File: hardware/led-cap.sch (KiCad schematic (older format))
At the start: 11 parts, among them IC1 ATTINY20-X, K1 CONN_3, K2 pgrm_top, K3 pgrm_bot, P1 battery, Q1 IRLML2402PbF, U1 MMA7660

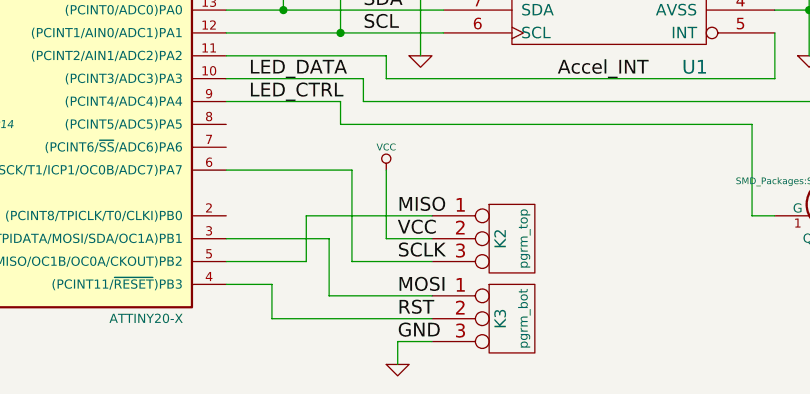
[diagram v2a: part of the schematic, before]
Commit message: Moving parts away from accelerometer
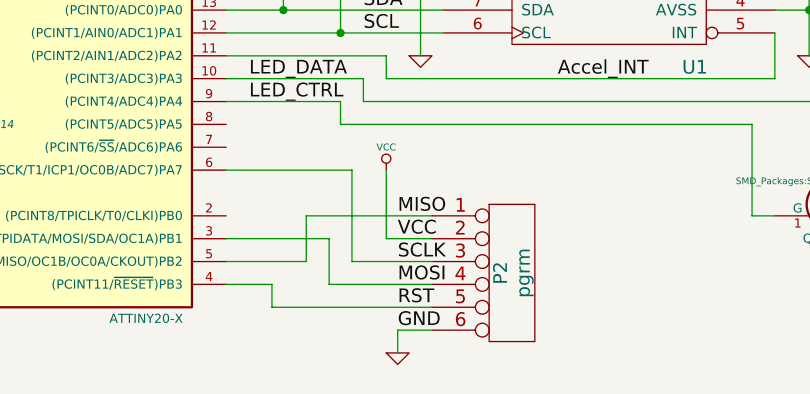
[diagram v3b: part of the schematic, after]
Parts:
- removed K2: pgrm_top, prgm:bcProgramHeader, symbol CONN_3
- removed K3: pgrm_bot, prgm:bcProgramHeader_bottom, symbol CONN_3
- added P2: pgrm, symbol CONN_6
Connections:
- net GND: now also P2.6
- net MISO: now also P2.1
- net MOSI: now also P2.4
- net RST: now also P2.5
- net SCLK: now also P2.3
- net VCC: now also P2.2
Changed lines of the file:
@@
 L GND #PWR07
 U 1 1 54E77FCD
-P 5750 5000
-F 0 "#PWR07" H 5750 5000 30  0001 C CNN
-F 1 "GND" H 5750 4930 30  0001 C CNN
-F 2 "" H 5750 5000 60  0000 C CNN
-F 3 "" H 5750 5000 60  0000 C CNN
-	1    5750 5000
+P 5750 4950
+F 0 "#PWR07" H 5750 4950 30  0001 C CNN
+F 1 "GND" H 5750 4880 30  0001 C CNN
+F 2 "" H 5750 4950 60  0000 C CNN
+F 3 "" H 5750 4950 60  0000 C CNN
+	1    5750 4950
 	1    0    0    -1
 $EndComp
@@
 	1    0    0    -1
 $EndComp
-$Comp
-L CONN_3 K2
-U 1 1 54EDFF11
-P 6250 4450
-F 0 "K2" V 6200 4450 50  0000 C CNN
-F 1 "pgrm_top" V 6300 4450 40  0000 C CNN
-F 2 "prgm:bcProgramHeader" H 6250 4450 60  0001 C CNN
-F 3 "" H 6250 4450 60  0000 C CNN
-	1    6250 4450
-	1    0    0    -1
-$EndComp
-$Comp
-L CONN_3 K3
-U 1 1 54EDFFA4
-P 6250 4800
-F 0 "K3" V 6200 4800 50  0000 C CNN
-F 1 "pgrm_bot" V 6300 4800 40  0000 C CNN
-F 2 "prgm:bcProgramHeader_bottom" H 6250 4800 60  0001 C CNN
-F 3 "" H 6250 4800 60  0000 C CNN
-	1    6250 4800
-	1    0    0    -1
-$EndComp
 Text Label 5600 3450 0    60   ~ 0
 SDA
@@
 Text Label 5750 4350 0    60   ~ 0
 MISO
-Text Label 5750 4700 0    60   ~ 0
+Text Label 5750 4650 0    60   ~ 0
 MOSI
-Text Label 5750 4800 0    60   ~ 0
+Text Label 5750 4750 0    60   ~ 0
 RST
-Text Label 5750 4900 0    60   ~ 0
+Text Label 5750 4850 0    60   ~ 0
 GND
 Text Label 5750 4450 0    60   ~ 0
@@
 	5550 4150 5000 4150
 Wire Wire Line
-	5900 4700 5450 4700
-Wire Wire Line
-	5450 4700 5450 4450
+	5900 4650 5450 4650
+Wire Wire Line
+	5450 4650 5450 4450
 Wire Wire Line
 	5450 4450 5000 4450
 Wire Wire Line
-	5900 4800 5200 4800
-Wire Wire Line
-	5200 4800 5200 4650
+	5900 4750 5200 4750
+Wire Wire Line
+	5200 4750 5200 4650
 Wire Wire Line
 	5200 4650 5000 4650
 Wire Wire Line
-	5900 4900 5750 4900
-Wire Wire Line
-	5750 4900 5750 5000
+	5900 4850 5750 4850
+Wire Wire Line
+	5750 4850 5750 4950
 Wire Wire Line
 	5000 3450 5950 3450
@@
 	7400 3150 7550 3150
 Connection ~ 7550 3450
+$Comp
+L CONN_6 P2
+U 1 1 54EFC480
+P 6250 4600
+F 0 "P2" V 6200 4600 60  0000 C CNN
+F 1 "pgrm" V 6300 4600 60  0000 C CNN
+F 2 "" H 6250 4600 60  0000 C CNN
+F 3 "" H 6250 4600 60  0000 C CNN
+	1    6250 4600
+	1    0    0    -1
+$EndComp
 $EndSCHEMATC

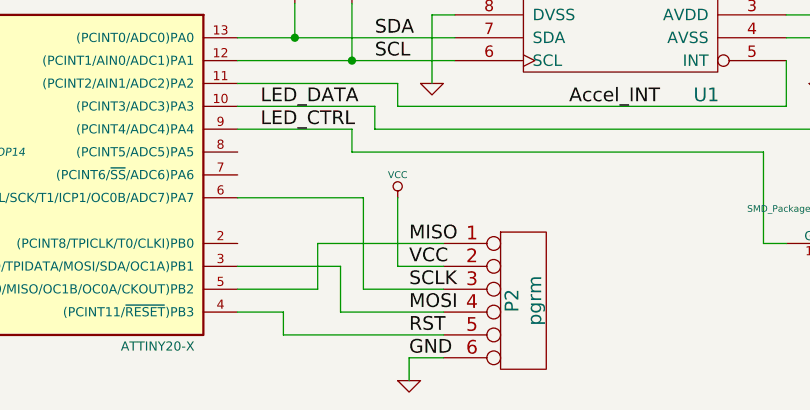
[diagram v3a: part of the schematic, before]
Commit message: Fixed programmer head from SPI to TPI
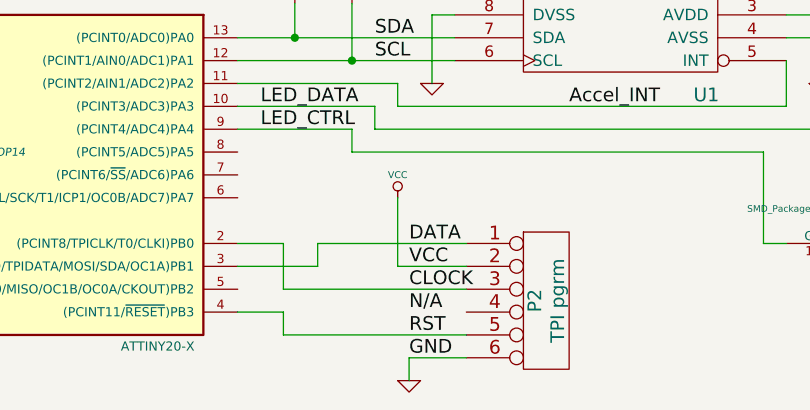
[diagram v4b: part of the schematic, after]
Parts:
- P2: value pgrm -> TPI pgrm
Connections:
- net CLOCK: now reaches IC1.2 ((PCINT8/TPICLK/T0/CLKI)PB0)
- net CLOCK: now also P2.3
- net MISO: no longer names the net of IC1.5 ((PCINT10/INT0/MISO/OC1B/OC0A/CKOUT)PB2)
- net MISO: no longer P2.1
- net MOSI: no longer names the net of P2.4
- net MOSI: no longer IC1.3 ((PCINT9/TPIDATA/MOSI/SDA/OC1A)PB1)
- net SCLK: no longer names the net of IC1.6 ((PCINT7/SCL/SCK/T1/ICP1/OC0B/ADC7)PA7)
- net SCLK: no longer P2.3
- new net DATA: IC1.3 ((PCINT9/TPIDATA/MOSI/SDA/OC1A)PB1), P2.1
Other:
- moved on the sheet: P2
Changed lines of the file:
@@
 Text Label 5600 3550 0    60   ~ 0
 SCL
-Text Label 5750 4350 0    60   ~ 0
-MISO
-Text Label 5750 4650 0    60   ~ 0
-MOSI
-Text Label 5750 4750 0    60   ~ 0
-RST
-Text Label 5750 4850 0    60   ~ 0
-GND
-Text Label 5750 4450 0    60   ~ 0
-VCC
-Text Label 5750 4550 0    60   ~ 0
-SCLK
 Text Label 5100 3750 0    60   ~ 0
 LED_DATA
@@
 	4000 3000 4000 3100
 Wire Wire Line
-	5000 4550 5350 4550
+	5350 4350 6000 4350
 Wire Wire Line
-	5350 4550 5350 4350
-Wire Wire Line
-	5350 4350 5900 4350
-Wire Wire Line
-	5900 4450 5700 4450
+	5700 4450 6000 4450
 Wire Wire Line
 	5700 4450 5700 4150
 Wire Wire Line
-	5900 4550 5550 4550
+	5200 4550 6000 4550
 Wire Wire Line
-	5550 4550 5550 4150
-Wire Wire Line
-	5550 4150 5000 4150
-Wire Wire Line
-	5900 4650 5450 4650
-Wire Wire Line
-	5450 4650 5450 4450
-Wire Wire Line
-	5450 4450 5000 4450
-Wire Wire Line
-	5900 4750 5200 4750
+	5200 4750 6000 4750
 Wire Wire Line
 	5200 4750 5200 4650
@@
 	5200 4650 5000 4650
 Wire Wire Line
-	5900 4850 5750 4850
+	5750 4850 6000 4850
 Wire Wire Line
 	5750 4850 5750 4950
@@
 L CONN_6 P2
 U 1 1 54EFC480
-P 6250 4600
-F 0 "P2" V 6200 4600 60  0000 C CNN
-F 1 "pgrm" V 6300 4600 60  0000 C CNN
-F 2 "" H 6250 4600 60  0000 C CNN
-F 3 "" H 6250 4600 60  0000 C CNN
-	1    6250 4600
+P 6350 4600
+F 0 "P2" V 6300 4600 60  0000 C CNN
+F 1 "TPI pgrm" V 6400 4600 60  0000 C CNN
+F 2 "" H 6350 4600 60  0000 C CNN
+F 3 "" H 6350 4600 60  0000 C CNN
+	1    6350 4600
 	1    0    0    -1
 $EndComp
+Text Label 5750 4850 0    60   ~ 0
+GND
+Text Label 5750 4750 0    60   ~ 0
+RST
+Text Label 5750 4650 0    60   ~ 0
+N/A
+Text Label 5750 4550 0    60   ~ 0
+CLOCK
+Text Label 5750 4450 0    60   ~ 0
+VCC
+Text Label 5750 4350 0    60   ~ 0
+DATA
+Wire Wire Line
+	5000 4350 5200 4350
+Wire Wire Line
+	5200 4350 5200 4550
+Wire Wire Line
+	5000 4450 5350 4450
+Wire Wire Line
+	5350 4450 5350 4350
 $EndSCHEMATC

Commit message: Fixing the mosfet
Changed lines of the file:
@@
 Text Label 5750 4750 0    60   ~ 0
 RST
-Text Label 5750 4650 0    60   ~ 0
-N/A
 Text Label 5750 4550 0    60   ~ 0
 CLOCK

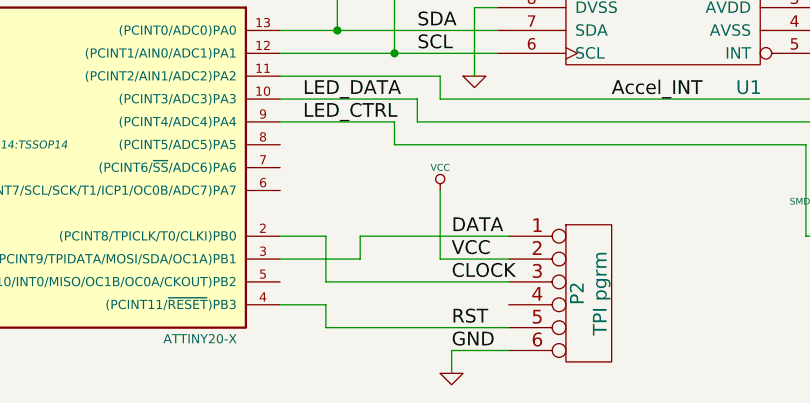
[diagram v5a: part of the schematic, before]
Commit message: Fixed pcb and schematic for TPI and new LED strips
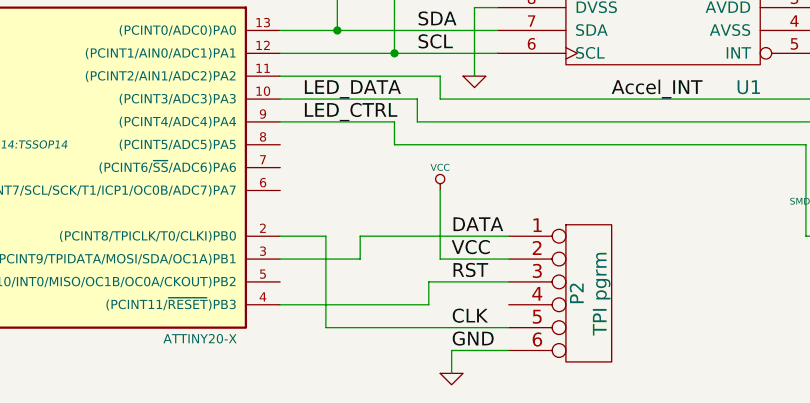
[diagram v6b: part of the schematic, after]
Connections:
- net RST: now also P2.3; no longer P2.5
- net CLOCK renamed CLK
- net CLK: now also P2.5; no longer P2.3
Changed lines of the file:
@@
 	5700 4450 5700 4150
 Wire Wire Line
-	5200 4550 6000 4550
+	5650 4550 6000 4550
 Wire Wire Line
 	5200 4750 6000 4750
 Wire Wire Line
-	5200 4750 5200 4650
-Wire Wire Line
-	5200 4650 5000 4650
+	5000 4650 5650 4650
 Wire Wire Line
 	5750 4850 6000 4850
@@
 GND
 Text Label 5750 4750 0    60   ~ 0
+CLK
+Text Label 5750 4550 0    60   ~ 0
 RST
-Text Label 5750 4550 0    60   ~ 0
-CLOCK
 Text Label 5750 4450 0    60   ~ 0
 VCC
@@
 	5000 4350 5200 4350
 Wire Wire Line
-	5200 4350 5200 4550
-Wire Wire Line
 	5000 4450 5350 4450
 Wire Wire Line
 	5350 4450 5350 4350
+Wire Wire Line
+	5200 4350 5200 4750
+Wire Wire Line
+	5650 4650 5650 4550
 $EndSCHEMATC
